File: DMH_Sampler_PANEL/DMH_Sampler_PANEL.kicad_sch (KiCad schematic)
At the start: 11 parts, among them J0 Panel_GND_Solder_Wire_Pad

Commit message: Panel experiments in progress
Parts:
- added H11: Size / End Pos, SynthStuff:Pot_Cutout_Small, symbol SynthStuff:MountingHole_Pot
- added H12: Start Pos, SynthStuff:Pot_Cutout_Small, symbol SynthStuff:MountingHole_Pot
- added H13: Speed, SynthStuff:Pot_Cutout_Small, symbol SynthStuff:MountingHole_Pot
- added H14: Trig Mode, SynthStuff:Toggle_Switch_TE_Cutout, symbol SynthStuff:MountingHole_ToggleSwitch
- added H15: Pb Mode, SynthStuff:Toggle_Switch_TE_Cutout, symbol SynthStuff:MountingHole_ToggleSwitch
- added H16: Rec Mode, SynthStuff:Toggle_Switch_TE_Cutout, symbol SynthStuff:MountingHole_ToggleSwitch
- added H17: CV Amt, SynthStuff:Toggle_Switch_TE_Cutout, symbol SynthStuff:MountingHole_ToggleSwitch
- added H18: Size Mode, SynthStuff:Toggle_Switch_TE_Cutout, symbol SynthStuff:MountingHole_ToggleSwitch
- added H19: Play, SynthStuff:MX_switch_Cutout, symbol Mechanical:MountingHole
- added H20: Rec, SynthStuff:MX_switch_Cutout, symbol Mechanical:MountingHole
- added J1: USB_C_Receptacle_USB2.0_16P, Connector_USB:USB_C_Receptacle_G-Switch_GT-USB-7051x, symbol Connector:USB_C_Receptacle_USB2.0_16P
- H10: value Audio Input -> Speed
- H8: value Audio Input -> Start
- H9: value Audio Input -> End
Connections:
- net GND: now also H10.1, H5.1, H6.1, H7.1, H8.1, H9.1, H11.1, H12.1, H13.1, H14.1, H15.1, H16.1, H17.1, H18.1
- new net: J1.A1 (GND), J1.A12 (GND), J1.B1 (GND), J1.B12 (GND)
- new net: J1.A4 (VBUS), J1.A9 (VBUS), J1.B4 (VBUS), J1.B9 (VBUS)

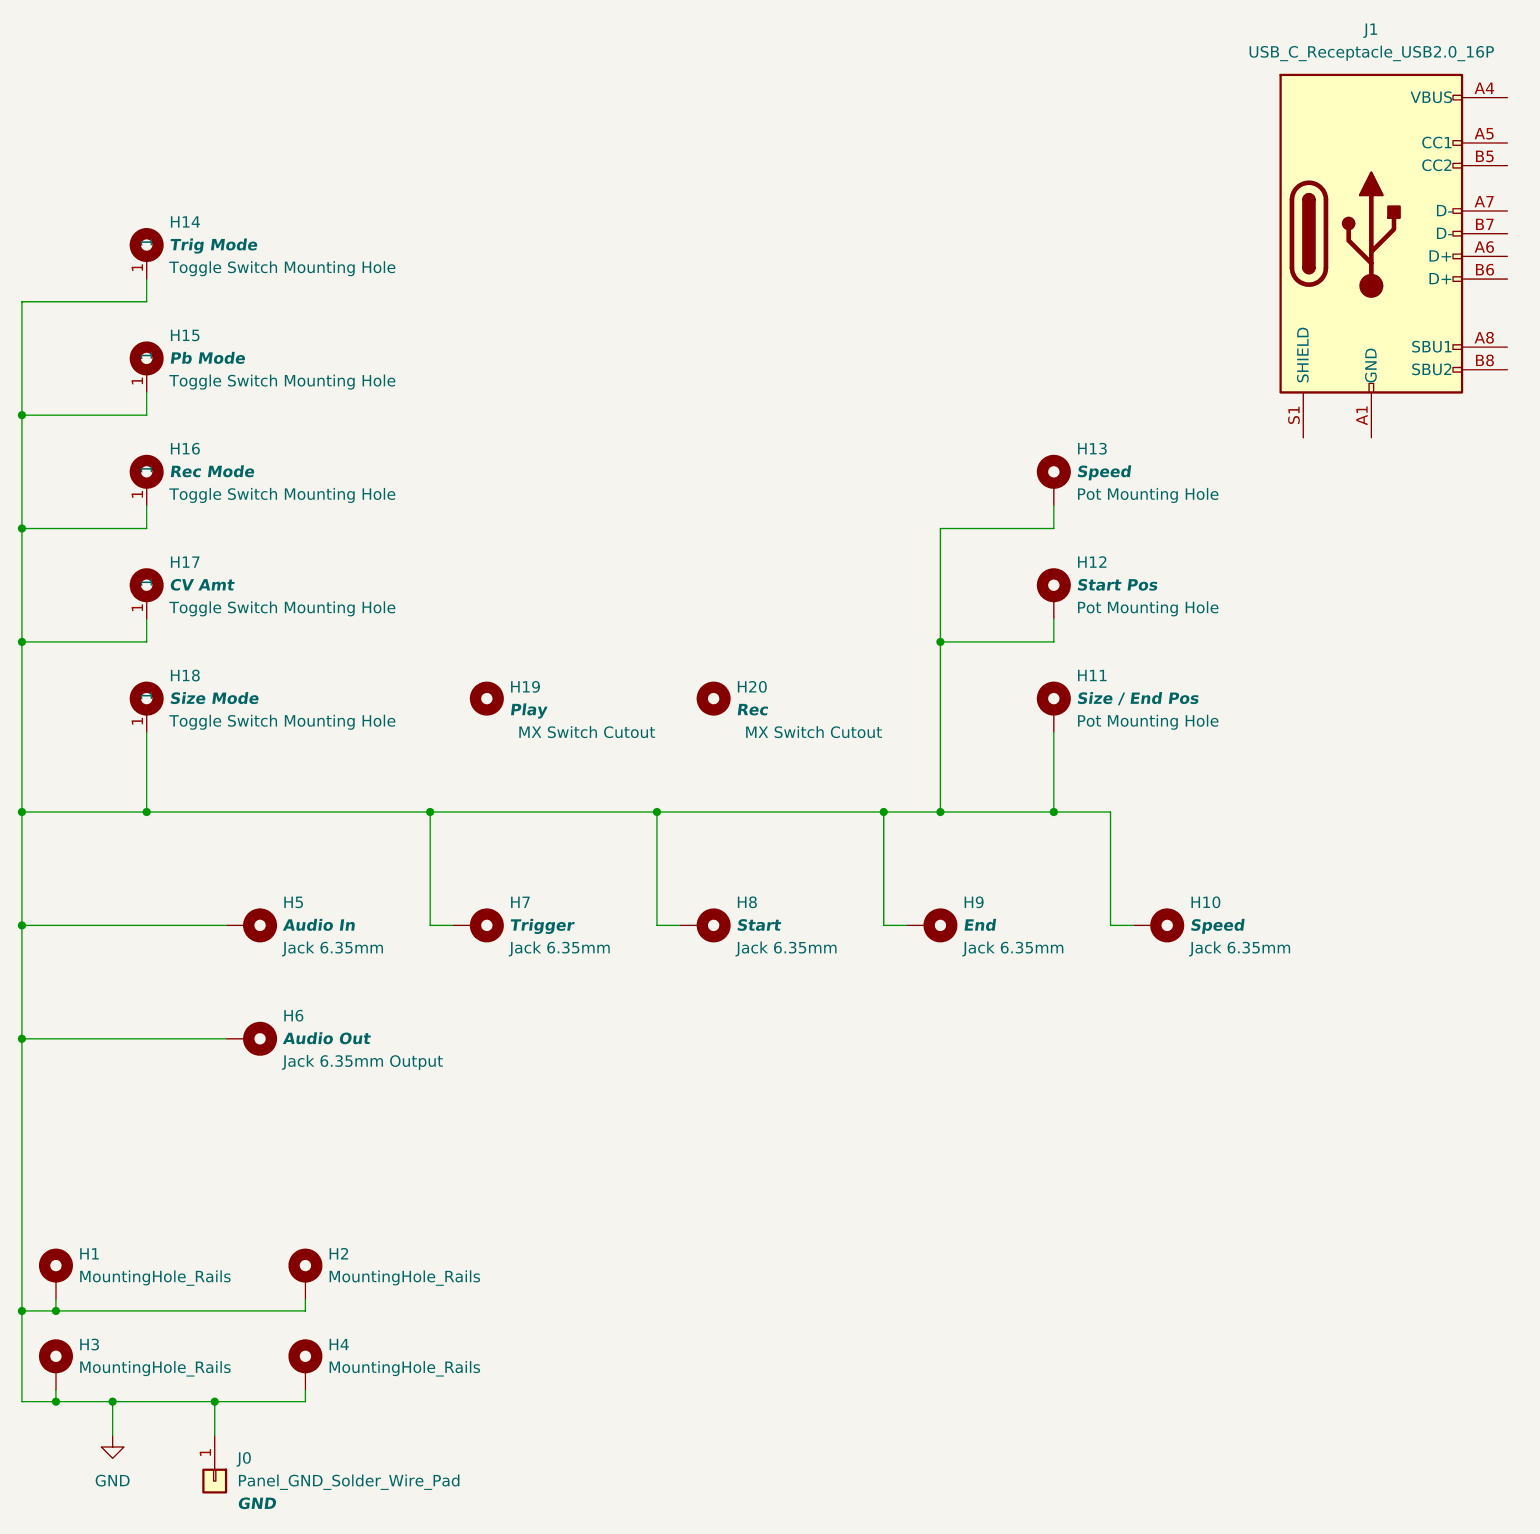
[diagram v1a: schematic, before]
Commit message: Designed front panel
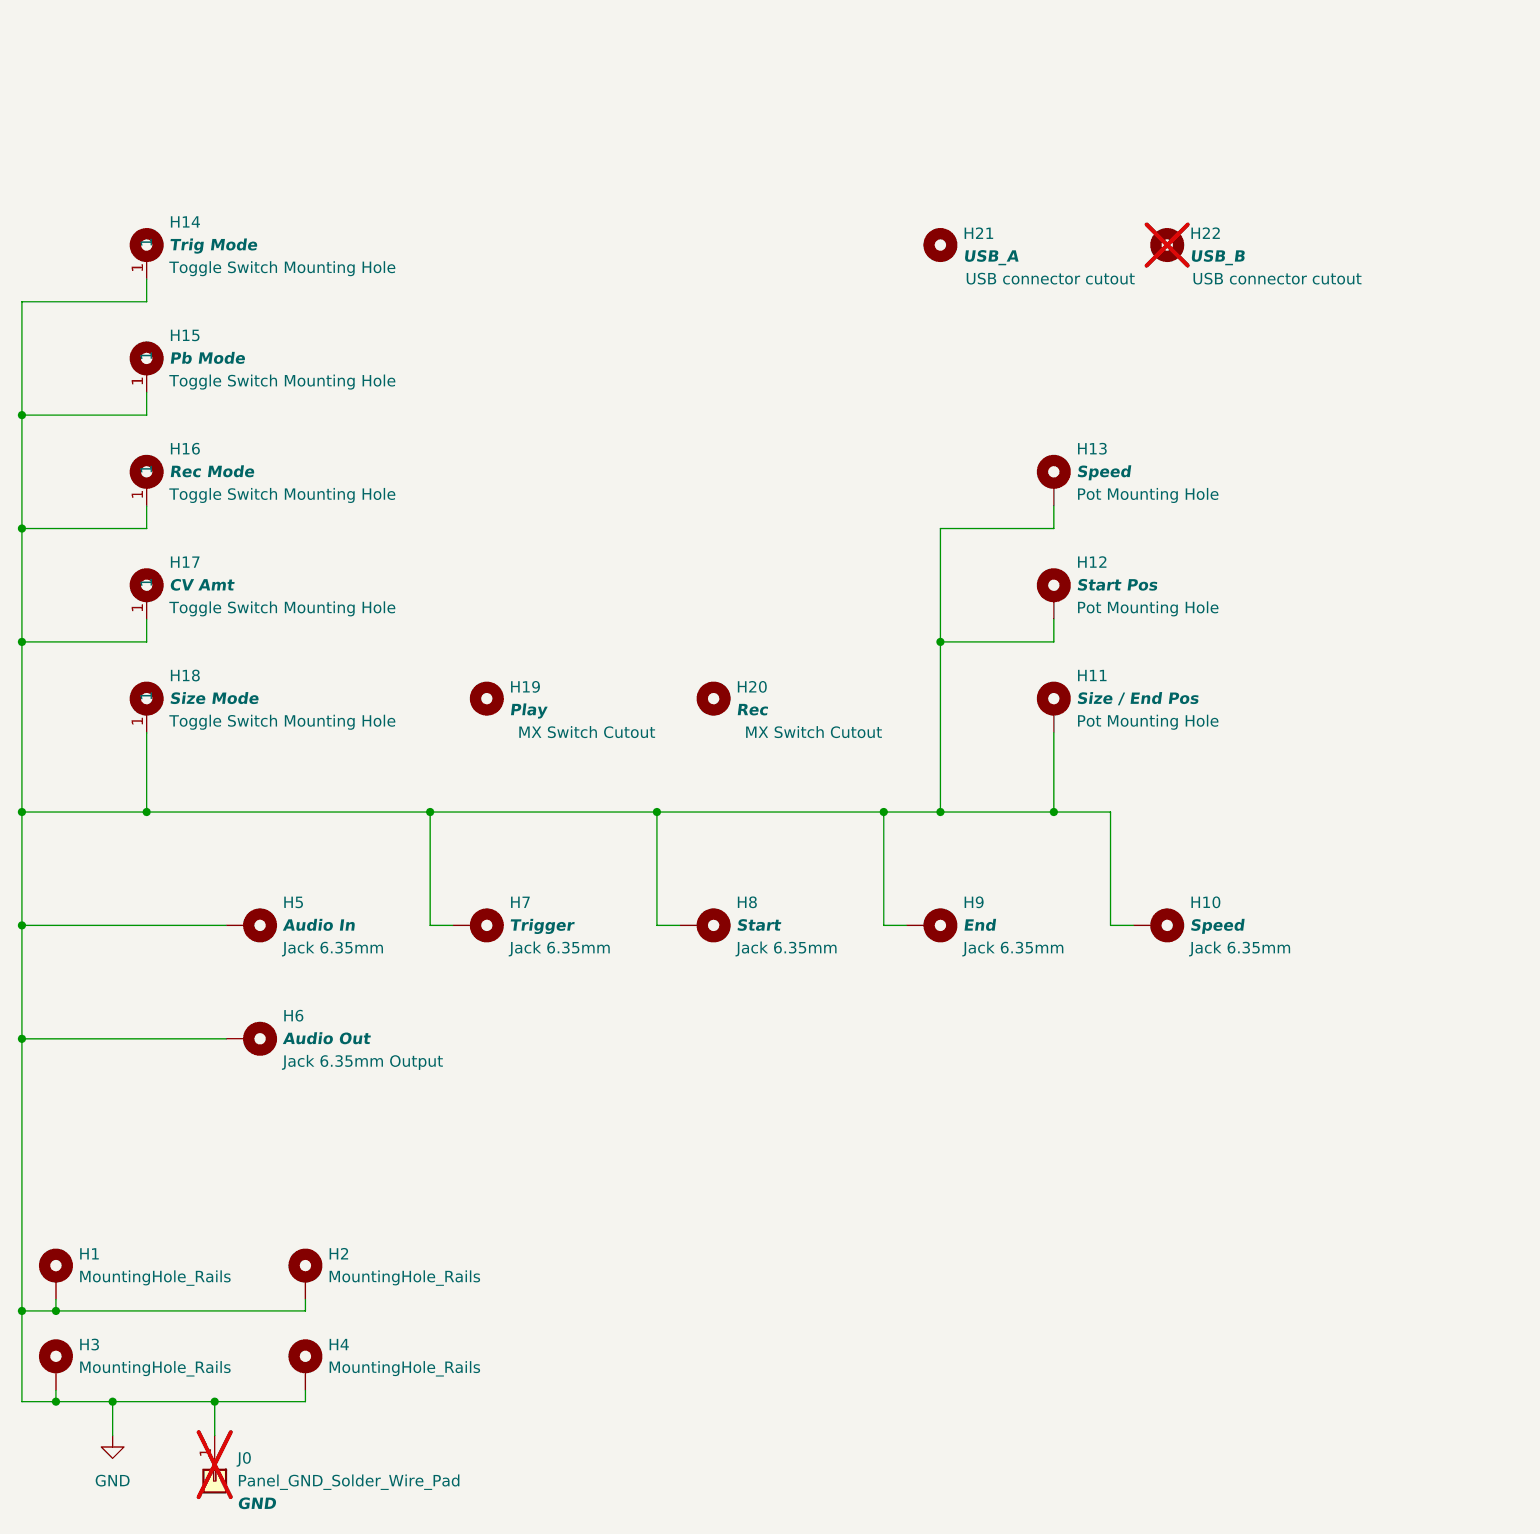
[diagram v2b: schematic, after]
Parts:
- removed J1: USB_C_Receptacle_USB2.0_16P, Connector_USB:USB_C_Receptacle_G-Switch_GT-USB-7051x, symbol Connector:USB_C_Receptacle_USB2.0_16P
- added H21: USB_A, SynthStuff:USB-A_Cutout, symbol Mechanical:MountingHole
- added H22: USB_B, SynthStuff:USB-B_Cutout, symbol Mechanical:MountingHole
- J0: now not fitted
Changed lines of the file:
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@@
 		(at 139.7 191.77 0)
 		(unit 1)
-		(exclude_from_sim yes)
+		(exclude_from_sim no)
 		(in_bom yes)
 		(on_board yes)
@@
 		(at 38.1 177.8 0)
 		(unit 1)
-		(exclude_from_sim yes)
+		(exclude_from_sim no)
 		(in_bom no)
 		(on_board yes)
@@
 		(at 38.1 139.7 0)
 		(unit 1)
-		(exclude_from_sim yes)
+		(exclude_from_sim no)
 		(in_bom no)
 		(on_board yes)
@@
 		(at 152.4 215.9 0)
 		(unit 1)
-		(exclude_from_sim yes)
+		(exclude_from_sim no)
 		(in_bom no)
 		(on_board yes)
@@
 		(at 38.1 165.1 0)
 		(unit 1)
-		(exclude_from_sim yes)
+		(exclude_from_sim no)
 		(in_bom no)
 		(on_board yes)
@@
 	)
 	(symbol
+		(lib_id "Mechanical:MountingHole")
+		(at 127 139.7 0)
+		(unit 1)
+		(exclude_from_sim no)
+		(in_bom no)
+		(on_board yes)
+		(dnp no)
+		(property "Reference" "H21"
+			(at 129.54 138.4299 0)
+			(effects
+				(font
+					(size 1.27 1.27)
+				)
+				(justify left)
+			)
+		)
+		(property "Value" "USB_A"
+			(at 129.54 140.9699 0)
+			(effects
+				(font
+					(size 1.27 1.27)
+					(thickness 0.254)
+					(bold yes)
+					(italic yes)
+				)
+				(justify left)
+			)
+		)
+		(property "Footprint" "SynthStuff:USB-A_Cutout"
+			(at 127 139.7 0)
+			(effects
+				(font
+					(size 1.27 1.27)
+				)
+				(hide yes)
+			)
+		)
+		(property "Datasheet" "~"
+			(at 127 139.7 0)
+			(effects
+				(font
+					(size 1.27 1.27)
+				)
+				(hide yes)
+			)
+		)
+		(property "Description" "USB connector cutout"
+			(at 129.794 143.51 0)
+			(effects
+				(font
+					(size 1.27 1.27)
+				)
+				(justify left)
+			)
+		)
+		(instances
+			(project ""
+				(path "/a552705f-a9fe-462e-9913-5cfcc08b233c"
+					(reference "H21")
+					(unit 1)
+				)
+			)
+		)
+	)
+	(symbol
 		(lib_id "SynthStuff:MountingHole_Jack6.35mm_v2")
 		(at 50.8 215.9 0)
 		(unit 1)
-		(exclude_from_sim yes)
+		(exclude_from_sim no)
 		(in_bom no)
 		(on_board yes)
@@
 		(at 127 215.9 0)
 		(unit 1)
-		(exclude_from_sim yes)
+		(exclude_from_sim no)
 		(in_bom no)
 		(on_board yes)
@@
 		(at 101.6 215.9 0)
 		(unit 1)
-		(exclude_from_sim yes)
+		(exclude_from_sim no)
 		(in_bom no)
 		(on_board yes)
@@
 		(at 50.8 228.6 0)
 		(unit 1)
-		(exclude_from_sim yes)
+		(exclude_from_sim no)
 		(in_bom no)
 		(on_board yes)
@@
 	)
 	(symbol
-		(lib_id "Connector:USB_C_Receptacle_USB2.0_16P")
-		(at 175.26 138.43 0)
-		(unit 1)
-		(exclude_from_sim no)
-		(in_bom yes)
-		(on_board yes)
-		(dnp no)
-		(fields_autoplaced yes)
-		(property "Reference" "J1"
-			(at 175.26 115.57 0)
-			(effects
-				(font
-					(size 1.27 1.27)
-				)
-			)
-		)
-		(property "Value" "USB_C_Receptacle_USB2.0_16P"
-			(at 175.26 118.11 0)
-			(effects
-				(font
-					(size 1.27 1.27)
-				)
-			)
-		)
-		(property "Footprint" "Connector_USB:USB_C_Receptacle_G-Switch_GT-USB-7051x"
-			(at 179.07 138.43 0)
-			(effects
-				(font
-					(size 1.27 1.27)
-				)
-				(hide yes)
-			)
-		)
-		(property "Datasheet" "https://www.usb.org/sites/default/files/documents/usb_type-c.zip"
-			(at 179.07 138.43 0)
-			(effects
-				(font
-					(size 1.27 1.27)
-				)
-				(hide yes)
-			)
-		)
-		(property "Description" "USB 2.0-only 16P Type-C Receptacle connector"
-			(at 175.26 138.43 0)
-			(effects
-				(font
-					(size 1.27 1.27)
-				)
-				(hide yes)
-			)
-		)
-		(pin "B4"
-		)
-		(pin "B12"
-		)
-		(pin "A1"
-		)
-		(pin "A5"
-		)
-		(pin "A12"
-		)
-		(pin "B5"
-		)
-		(pin "A7"
-		)
-		(pin "B7"
-		)
-		(pin "B8"
-		)
-		(pin "A4"
-		)
-		(pin "A8"
-		)
-		(pin "S1"
-		)
-		(pin "B1"
-		)
-		(pin "A9"
-		)
-		(pin "A6"
-		)
-		(pin "B6"
-		)
-		(pin "B9"
-		)
-		(instances
-			(project ""
-				(path "/a552705f-a9fe-462e-9913-5cfcc08b233c"
-					(reference "J1")
-					(unit 1)
-				)
-			)
-		)
-	)
-	(symbol
 		(lib_id "SynthStuff:MountingHole_Pot")
 		(at 139.7 179.07 0)
 		(unit 1)
-		(exclude_from_sim yes)
+		(exclude_from_sim no)
 		(in_bom yes)
 		(on_board yes)
@@
 		(at 139.7 166.37 0)
 		(unit 1)
-		(exclude_from_sim yes)
+		(exclude_from_sim no)
 		(in_bom yes)
 		(on_board yes)
@@
 		(at 38.1 190.5 0)
 		(unit 1)
-		(exclude_from_sim yes)
+		(exclude_from_sim no)
 		(in_bom no)
 		(on_board yes)
@@
 	)
 	(symbol
+		(lib_id "Mechanical:MountingHole")
+		(at 152.4 139.7 0)
+		(unit 1)
+		(exclude_from_sim no)
+		(in_bom no)
+		(on_board no)
+		(dnp yes)
+		(property "Reference" "H22"
+			(at 154.94 138.4299 0)
+			(effects
+				(font
+					(size 1.27 1.27)
+				)
+				(justify left)
+			)
+		)
+		(property "Value" "USB_B"
+			(at 154.94 140.9699 0)
+			(effects
+				(font
+					(size 1.27 1.27)
+					(thickness 0.254)
+					(bold yes)
+					(italic yes)
+				)
+				(justify left)
+			)
+		)
+		(property "Footprint" "SynthStuff:USB-B_Cutout"
+			(at 152.4 139.7 0)
+			(effects
+				(font
+					(size 1.27 1.27)
+				)
+				(hide yes)
+			)
+		)
+		(property "Datasheet" "~"
+			(at 152.4 139.7 0)
+			(effects
+				(font
+					(size 1.27 1.27)
+				)
+				(hide yes)
+			)
+		)
+		(property "Description" "USB connector cutout"
+			(at 155.194 143.51 0)
+			(effects
+				(font
+					(size 1.27 1.27)
+				)
+				(justify left)
+			)
+		)
+		(instances
+			(project "DMH_Sampler_PANEL"
+				(path "/a552705f-a9fe-462e-9913-5cfcc08b233c"
+					(reference "H22")
+					(unit 1)
+				)
+			)
+		)
+	)
+	(symbol
 		(lib_id "SynthStuff:MountingHole_ToggleSwitch")
 		(at 38.1 152.4 0)
 		(unit 1)
-		(exclude_from_sim yes)
+		(exclude_from_sim no)
 		(in_bom no)
 		(on_board yes)
@@
 		(at 76.2 215.9 0)
 		(unit 1)
-		(exclude_from_sim yes)
+		(exclude_from_sim no)
 		(in_bom no)
 		(on_board yes)
@@
 		(exclude_from_sim no)
 		(in_bom no)
-		(on_board yes)
-		(dnp no)
+		(on_board no)
+		(dnp yes)
 		(fields_autoplaced yes)
 		(property "Reference" "J0"

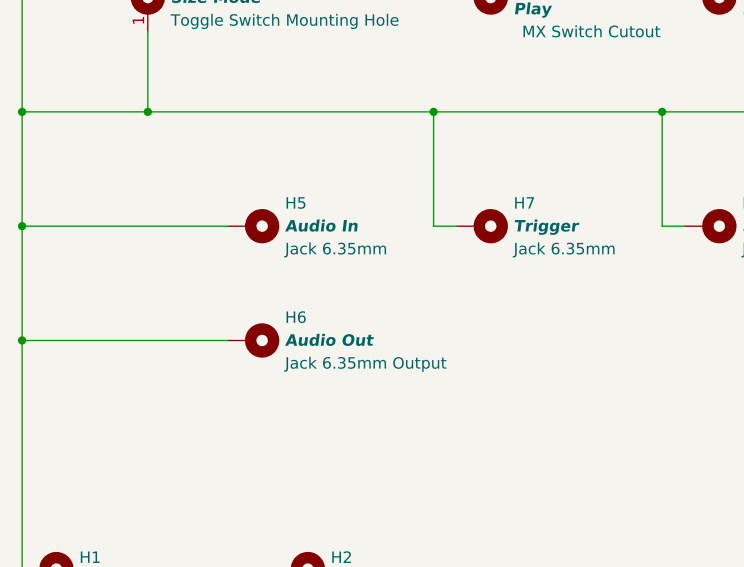
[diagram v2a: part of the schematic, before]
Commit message: Added solder mask cutouts for LEDs
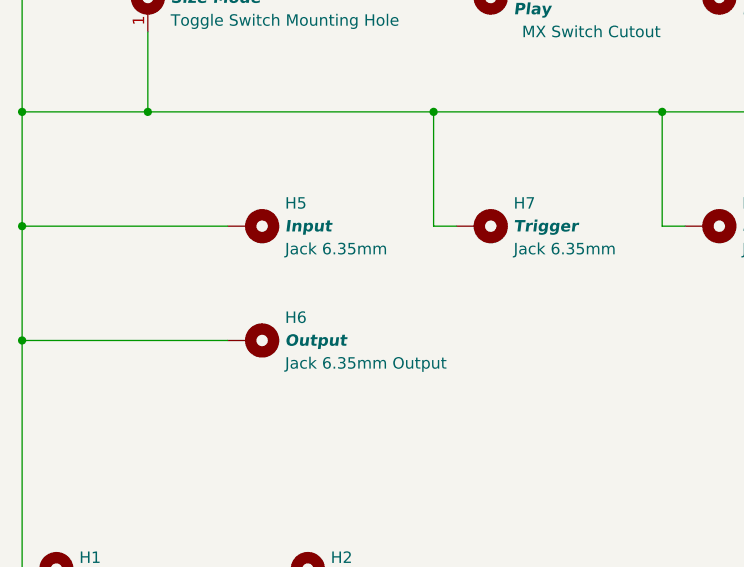
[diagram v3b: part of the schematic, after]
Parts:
- H5: value Audio In -> Input
- H6: value Audio Out -> Output
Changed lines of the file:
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@@
 			)
 		)
-		(property "Value" "Audio In"
+		(property "Value" "Input"
 			(at 53.34 215.9 0)
 			(effects
@@
 			)
 		)
-		(property "Value" "Audio Out"
+		(property "Value" "Output"
 			(at 53.34 228.6 0)
 			(effects
